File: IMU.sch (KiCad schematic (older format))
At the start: 24 parts

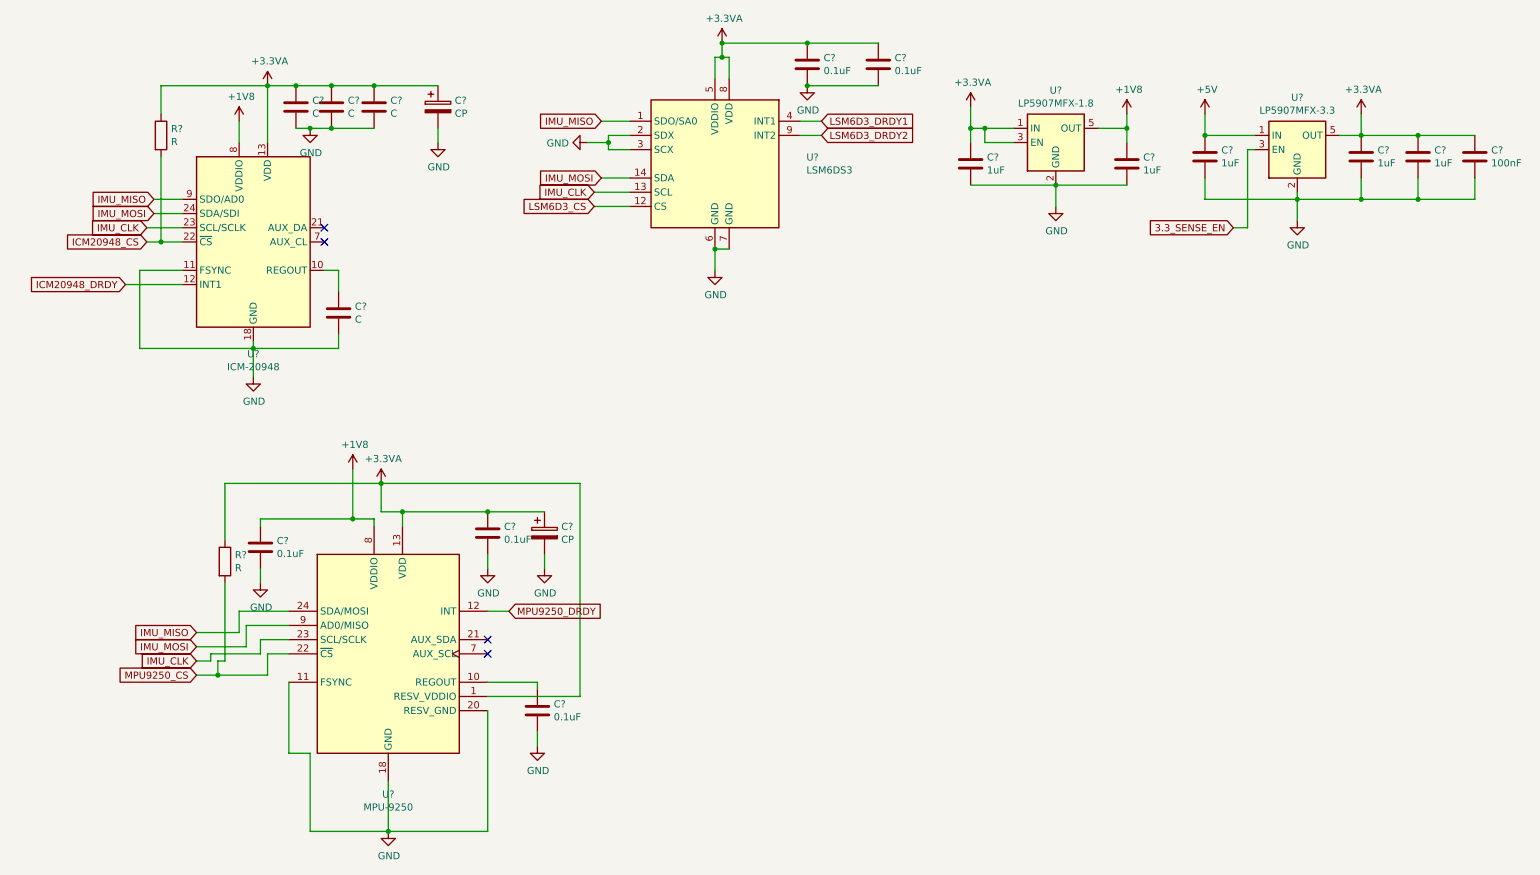
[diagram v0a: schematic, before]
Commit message: 4 layer add
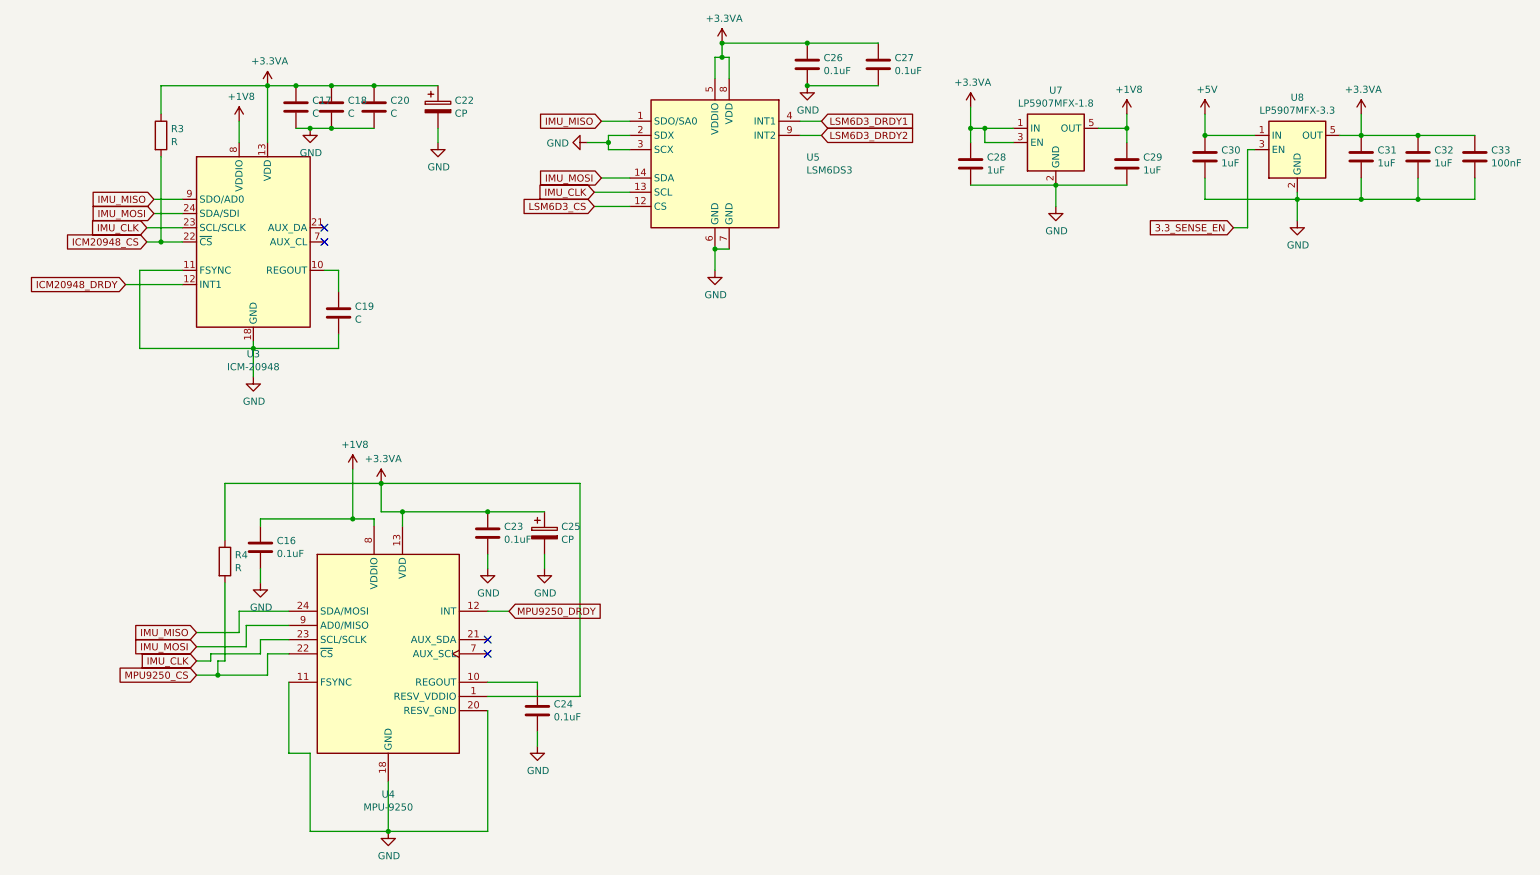
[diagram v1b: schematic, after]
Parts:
- gave numbers to parts that had none: 24

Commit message: a
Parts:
- removed R3, R4: R, Resistor_SMD:R_0402_1005Metric, symbol Device:R
- added C42: 0.1uF, Capacitor_SMD:C_0603_1608Metric, symbol Device:C
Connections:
- net +1V8: now also C42.1
- net GND: now also C42.2
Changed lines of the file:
@@
 Wire Wire Line
 	2000 5450 1900 5450
-Wire Wire Line
-	1900 5550 2050 5550
-Wire Wire Line
-	2050 5550 2050 5450
-Wire Wire Line
-	2050 5450 2100 5450
 Text GLabel 4100 5100 2    50   Input ~ 0
 MPU9250_DRDY
-$Comp
-L Device:R R?
-U 1 1 5F5A50E3
-P 2100 4750
-AR Path="/5F3218EE/5F5A50E3" Ref="R?"  Part="1"
-AR Path="/5F5A50E3" Ref="R?"  Part="1"
-AR Path="/5F584BC5/5F5A50E3" Ref="R4"  Part="1"
-AR Path="/5F5AF088/5F5A50E3" Ref="R?"  Part="1"
-F 0 "R4" H 2170 4796 50  0000 L CNN
-F 1 "R" H 2170 4705 50  0000 L CNN
-F 2 "Resistor_SMD:R_0402_1005Metric" V 2030 4750 50  0001 C CNN
-F 3 "~" H 2100 4750 50  0001 C CNN
-	1    2100 4750
-	1    0    0    -1
-$EndComp
-Wire Wire Line
-	2100 4900 2100 5450
 Wire Wire Line
 	3350 4400 3200 4400
-Wire Wire Line
-	2100 4200 2100 4600
 Wire Wire Line
 	4300 6050 4300 5950
@@
 	2550 6100 2700 6100
 Wire Wire Line
-	2050 5550 2400 5550
-Wire Wire Line
 	2400 5550 2400 5400
 Wire Wire Line
 	2400 5400 2550 5400
-Connection ~ 2050 5550
 Wire Wire Line
 	4100 5100 3950 5100
@@
 	4600 4200 3200 4200
 Connection ~ 3200 4200
-Wire Wire Line
-	2100 4200 3200 4200
 Wire Wire Line
 	3950 5600 4300 5600
@@
 $EndComp
 Wire Wire Line
-	2200 1800 2200 1650
-$Comp
-L Device:R R?
-U 1 1 5F5A522A
-P 1650 1750
-AR Path="/5F3218EE/5F5A522A" Ref="R?"  Part="1"
-AR Path="/5F5A522A" Ref="R?"  Part="1"
-AR Path="/5F584BC5/5F5A522A" Ref="R3"  Part="1"
-AR Path="/5F5AF088/5F5A522A" Ref="R?"  Part="1"
-F 0 "R3" H 1720 1796 50  0000 L CNN
-F 1 "R" H 1720 1705 50  0000 L CNN
-F 2 "Resistor_SMD:R_0402_1005Metric" V 1580 1750 50  0001 C CNN
-F 3 "~" H 1650 1750 50  0001 C CNN
-	1    1650 1750
-	1    0    0    -1
-$EndComp
+	2200 1800 2200 1700
 Wire Wire Line
 	2400 1400 2600 1400
-Wire Wire Line
-	1550 2500 1650 2500
-Wire Wire Line
-	1650 1400 1650 1600
-Wire Wire Line
-	1650 1400 2400 1400
-Wire Wire Line
-	1650 1900 1650 2500
-Connection ~ 1650 2500
-Wire Wire Line
-	1650 2500 1800 2500
 $Comp
 L Device:CP C?
@@
 Wire Wire Line
 	7450 1700 7650 1700
+$Comp
+L Device:C C?
+U 1 1 5F5A8609
+P 2050 1700
+AR Path="/5F3218EE/5F5A8609" Ref="C?"  Part="1"
+AR Path="/5F5A8609" Ref="C?"  Part="1"
+AR Path="/5F584BC5/5F5A8609" Ref="C42"  Part="1"
+AR Path="/5F5AF088/5F5A8609" Ref="C?"  Part="1"
+F 0 "C42" H 2165 1746 50  0000 L CNN
+F 1 "0.1uF" H 2165 1655 50  0000 L CNN
+F 2 "Capacitor_SMD:C_0603_1608Metric" H 2088 1550 50  0001 C CNN
+F 3 "~" H 2050 1700 50  0001 C CNN
+	1    2050 1700
+	0    1    1    0
+$EndComp
+Wire Wire Line
+	1900 1700 1800 1700
+$Comp
+L power:GND #PWR?
+U 1 1 5F5A8610
+P 1800 1700
+AR Path="/5F3218EE/5F5A8610" Ref="#PWR?"  Part="1"
+AR Path="/5F5A8610" Ref="#PWR?"  Part="1"
+AR Path="/5F584BC5/5F5A8610" Ref="#PWR0182"  Part="1"
+AR Path="/5F5AF088/5F5A8610" Ref="#PWR?"  Part="1"
+F 0 "#PWR0182" H 1800 1450 50  0001 C CNN
+F 1 "GND" H 1805 1527 50  0000 C CNN
+F 2 "" H 1800 1700 50  0001 C CNN
+F 3 "" H 1800 1700 50  0001 C CNN
+	1    1800 1700
+	0    1    1    0
+$EndComp
+Wire Wire Line
+	1550 2500 1800 2500
+Connection ~ 2200 1700
+Wire Wire Line
+	2200 1700 2200 1650
+Wire Wire Line
+	1900 5550 2400 5550
 $EndSCHEMATC

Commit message: finish board
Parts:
- added J23: Conn_01x10_Male, Connector_PinHeader_2.54mm:PinHeader_1x10_P2.54mm_Vertical, symbol Connector:Conn_01x10_Male
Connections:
- net +5V: now also J23.1 (Pin_1)
- net 3.3_SENSE_EN: now also J23.10 (Pin_10)
- net GND: now also J23.2 (Pin_2)
- net ICM20948_CS: now also J23.8 (Pin_8)
- net IMU_CLK: now also J23.3 (Pin_3)
- net IMU_MISO: now also J23.7 (Pin_7)
- net IMU_MOSI: now also J23.4 (Pin_4)
- net LSM6D3_CS: now also J23.6 (Pin_6)
- net MPU9250_CS: now also J23.5 (Pin_5)
- new net EXTERNAL_MPU_CS: J23.9 (Pin_9)
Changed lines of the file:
@@
 Wire Wire Line
 	1900 5550 2400 5550
+$Comp
+L power:+5V #PWR?
+U 1 1 5F649538
+P 5450 3350
+AR Path="/5F3218EE/5F649538" Ref="#PWR?"  Part="1"
+AR Path="/5F649538" Ref="#PWR?"  Part="1"
+AR Path="/5F584BC5/5F649538" Ref="#PWR0188"  Part="1"
+AR Path="/5F5AF088/5F649538" Ref="#PWR?"  Part="1"
+F 0 "#PWR0188" H 5450 3200 50  0001 C CNN
+F 1 "+5V" H 5465 3523 50  0000 C CNN
+F 2 "" H 5450 3350 50  0001 C CNN
+F 3 "" H 5450 3350 50  0001 C CNN
+	1    5450 3350
+	1    0    0    -1
+$EndComp
+Wire Wire Line
+	5350 3500 5450 3500
+Wire Wire Line
+	5450 3500 5450 3350
+$Comp
+L power:GND #PWR0189
+U 1 1 5F65131E
+P 5500 3600
+F 0 "#PWR0189" H 5500 3350 50  0001 C CNN
+F 1 "GND" V 5505 3472 50  0000 R CNN
+F 2 "" H 5500 3600 50  0001 C CNN
+F 3 "" H 5500 3600 50  0001 C CNN
+	1    5500 3600
+	0    -1   -1   0
+$EndComp
+Wire Wire Line
+	5350 3600 5500 3600
+$Comp
+L Connector:Conn_01x10_Male J23
+U 1 1 5F659907
+P 5150 3900
+F 0 "J23" H 5258 4481 50  0000 C CNN
+F 1 "Conn_01x10_Male" H 5258 4390 50  0000 C CNN
+F 2 "Connector_PinHeader_2.54mm:PinHeader_1x10_P2.54mm_Vertical" H 5150 3900 50  0001 C CNN
+F 3 "~" H 5150 3900 50  0001 C CNN
+	1    5150 3900
+	1    0    0    -1
+$EndComp
+Text GLabel 5350 3800 2    50   Input ~ 0
+IMU_MOSI
+Text GLabel 5350 4100 2    50   Input ~ 0
+IMU_MISO
+Text GLabel 5350 3700 2    50   Input ~ 0
+IMU_CLK
+Text GLabel 5350 4300 2    50   Input ~ 0
+EXTERNAL_MPU_CS
+Text GLabel 5600 4200 2    50   Input ~ 0
+ICM20948_CS
+Wire Wire Line
+	5600 4200 5350 4200
+Text GLabel 5600 4000 2    50   Input ~ 0
+LSM6D3_CS
+Wire Wire Line
+	5600 4000 5350 4000
+Text GLabel 5850 3900 2    50   Input ~ 0
+MPU9250_CS
+Wire Wire Line
+	5850 3900 5350 3900
+Text GLabel 5500 4400 2    50   Input ~ 0
+3.3_SENSE_EN
+Wire Wire Line
+	5350 4400 5500 4400
 $EndSCHEMATC
